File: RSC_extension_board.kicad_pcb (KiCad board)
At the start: 2 copper layers, 65 x 56.5 mm, 110 parts, among them J1 NPTC202KFMS-RC, J10 Conn_01x04, J11 Conn_01x03, J12 Conn_01x03, J13 Conn_01x10, J16 USB_C_Receptacle_PowerOnly_6P, J2 Conn_01x02, J4 TSM-120-01-L-DH-A-K-TR, J5 Conn_01x02, J6 Conn_01x03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

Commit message: generic 2.54mm headers and testPads excluded from BOM
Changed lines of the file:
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@@
 		(sheetname "/Buck converter/")
 		(sheetfile "buck_converter.kicad_sch")
-		(attr smd)
+		(attr smd dnp)
 		(fp_line
 			(start -0.254724 0.5225)
@@
 		(sheetname "/")
 		(sheetfile "RSC_extension_board.kicad_sch")
-		(attr through_hole)
+		(attr through_hole exclude_from_bom)
 		(fp_line
 			(start -1.33 24.19)
@@
 		(sheetname "/Buck converter/")
 		(sheetfile "buck_converter.kicad_sch")
-		(attr smd)
+		(attr smd dnp)
 		(fp_line
 			(start -0.254724 -0.5225)
@@
 		(sheetname "/Buck converter/")
 		(sheetfile "buck_converter.kicad_sch")
-		(attr smd)
+		(attr smd dnp)
 		(fp_line
 			(start -0.254724 0.5225)
@@
 		(sheetname "/")
 		(sheetfile "RSC_extension_board.kicad_sch")
-		(attr through_hole)
+		(attr through_hole exclude_from_bom)
 		(fp_line
 			(start -1.38 6.46)
@@
 		(sheetname "/")
 		(sheetfile "RSC_extension_board.kicad_sch")
-		(attr through_hole)
+		(attr through_hole exclude_from_bom)
 		(fp_line
 			(start -1.38 6.46)
@@
 		(property "Reference" "L1"
 			(at 0 0 90)
-			(layer "Cmts.User")
+			(layer "F.SilkS")
 			(effects
 				(font
@@
 		(sheetname "/Buck converter/")
 		(sheetfile "buck_converter.kicad_sch")
-		(attr smd)
+		(attr smd dnp)
 		(fp_line
 			(start -0.254724 -0.5225)
@@
 		(sheetname "/")
 		(sheetfile "RSC_extension_board.kicad_sch")
-		(attr through_hole)
+		(attr through_hole exclude_from_bom)
 		(fp_line
 			(start -1.38 -1.38)
@@
 		(sheetname "/")
 		(sheetfile "RSC_extension_board.kicad_sch")
-		(attr through_hole)
+		(attr through_hole exclude_from_bom)
 		(fp_line
 			(start -1.38 6.46)
@@
 		(sheetname "/Buck converter/")
 		(sheetfile "buck_converter.kicad_sch")
-		(attr smd)
+		(attr smd dnp)
 		(fp_line
 			(start -0.254724 -0.5225)
@@
 		(property "Reference" "L2"
 			(at 0 0 90)
-			(layer "Cmts.User")
+			(layer "F.SilkS")
 			(effects
 				(font
@@
 		(sheetname "/")
 		(sheetfile "RSC_extension_board.kicad_sch")
-		(attr through_hole)
+		(attr through_hole exclude_from_bom)
 		(fp_line
 			(start -1.38 6.46)
@@
 		(sheetname "/USB_power/")
 		(sheetfile "USB_power.kicad_sch")
-		(attr through_hole)
+		(attr through_hole exclude_from_bom)
 		(fp_line
 			(start -1.38 -1.38)
@@
 		(sheetname "/")
 		(sheetfile "RSC_extension_board.kicad_sch")
-		(attr through_hole)
+		(attr through_hole exclude_from_bom)
 		(fp_line
 			(start -1.38 -1.38)
@@
 		(sheetname "/Buck converter/")
 		(sheetfile "buck_converter.kicad_sch")
-		(attr smd)
+		(attr smd dnp)
 		(fp_line
 			(start -0.254724 0.5225)
@@
 		(sheetname "/")
 		(sheetfile "RSC_extension_board.kicad_sch")
-		(attr through_hole)
+		(attr through_hole exclude_from_bom)
 		(fp_line
 			(start -1.38 6.46)
@@
 		(sheetname "/")
 		(sheetfile "RSC_extension_board.kicad_sch")
-		(attr board_only exclude_from_pos_files)
+		(attr board_only exclude_from_pos_files exclude_from_bom)
 		(fp_poly
 			(pts
@@
 		(property "Reference" "J4"
 			(at -1.27 -4.19 0)
-			(layer "Cmts.User")
+			(layer "F.SilkS")
 			(effects
 				(font
@@
 		(sheetname "/")
 		(sheetfile "RSC_extension_board.kicad_sch")
-		(attr through_hole)
+		(attr through_hole exclude_from_bom)
 		(fp_line
 			(start -1.38 -1.38)
@@
 		(sheetname "/Buck converter/")
 		(sheetfile "buck_converter.kicad_sch")
-		(attr exclude_from_pos_files)
+		(attr exclude_from_pos_files exclude_from_bom)
 		(fp_circle
 			(center 0 0)
@@
 		(sheetname "/Buck converter/")
 		(sheetfile "buck_converter.kicad_sch")
-		(attr exclude_from_pos_files)
+		(attr exclude_from_pos_files exclude_from_bom)
 		(fp_circle
 			(center 0 0)
@@
 		(sheetname "/Buck converter/")
 		(sheetfile "buck_converter.kicad_sch")
-		(attr exclude_from_pos_files)
+		(attr exclude_from_pos_files exclude_from_bom)
 		(fp_circle
 			(center 0 0)
@@
 		(sheetname "/Buck converter/")
 		(sheetfile "buck_converter.kicad_sch")
-		(attr exclude_from_pos_files)
+		(attr exclude_from_pos_files exclude_from_bom)
 		(fp_circle
 			(center 0 0)
@@
 		(sheetname "/Buck converter/")
 		(sheetfile "buck_converter.kicad_sch")
-		(attr exclude_from_pos_files)
+		(attr exclude_from_pos_files exclude_from_bom)
 		(fp_circle
 			(center 0 0)
@@
 		(sheetname "/Buck converter/")
 		(sheetfile "buck_converter.kicad_sch")
-		(attr exclude_from_pos_files)
+		(attr exclude_from_pos_files exclude_from_bom)
 		(fp_circle
 			(center 0 0)
@@
 		(sheetname "/Buck converter/")
 		(sheetfile "buck_converter.kicad_sch")
-		(attr exclude_from_pos_files)
+		(attr exclude_from_pos_files exclude_from_bom)
 		(fp_circle
 			(center 0 0)
@@
 		(sheetname "/Buck converter/")
 		(sheetfile "buck_converter.kicad_sch")
-		(attr exclude_from_pos_files)
+		(attr exclude_from_pos_files exclude_from_bom)
 		(fp_circle
 			(center 0 0)
@@
 		(sheetname "/Buck converter/")
 		(sheetfile "buck_converter.kicad_sch")
-		(attr exclude_from_pos_files)
+		(attr exclude_from_pos_files exclude_from_bom)
 		(fp_circle
 			(center 0 0)
@@
 		(sheetname "/Buck converter/")
 		(sheetfile "buck_converter.kicad_sch")
-		(attr exclude_from_pos_files)
+		(attr exclude_from_pos_files exclude_from_bom)
 		(fp_circle
 			(center 0 0)
@@
 		(sheetname "/Buck converter/")
 		(sheetfile "buck_converter.kicad_sch")
-		(attr exclude_from_pos_files)
+		(attr exclude_from_pos_files exclude_from_bom)
 		(fp_circle
 			(center 0 0)
@@
 		(sheetname "/Buck converter/")
 		(sheetfile "buck_converter.kicad_sch")
-		(attr exclude_from_pos_files)
+		(attr exclude_from_pos_files exclude_from_bom)
 		(fp_circle
 			(center 0 0)
@@
 		(sheetname "/Buck converter/")
 		(sheetfile "buck_converter.kicad_sch")
-		(attr exclude_from_pos_files)
+		(attr exclude_from_pos_files exclude_from_bom)
 		(fp_circle
 			(center 0 0)
@@
 		(sheetname "/Buck converter/")
 		(sheetfile "buck_converter.kicad_sch")
-		(attr exclude_from_pos_files)
+		(attr exclude_from_pos_files exclude_from_bom)
 		(fp_circle
 			(center 0 0)
@@
 		(sheetname "/Buck converter/")
 		(sheetfile "buck_converter.kicad_sch")
-		(attr exclude_from_pos_files)
+		(attr exclude_from_pos_files exclude_from_bom)
 		(fp_circle
 			(center 0 0)
@@
 		(sheetname "/Buck converter/")
 		(sheetfile "buck_converter.kicad_sch")
-		(attr exclude_from_pos_files)
+		(attr exclude_from_pos_files exclude_from_bom)
 		(fp_circle
 			(center 0 0)

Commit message: J4 connector had correct footprint but false component name
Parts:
- J4: value TSM-120-01-L-DH-A-K-TR -> TSM-120-02-F-DH
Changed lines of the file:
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@@
 			)
 		)
-		(property "Value" "TSM-120-01-L-DH-A-K-TR"
+		(property "Value" "TSM-120-02-F-DH"
 			(at 0 0 0)
 			(layer "F.SilkS")
@@
 			)
 		)
-		(property "Manufacturer_Part_Number" "TSM-120-01-L-DH-A-K-TR"
+		(property "Manufacturer_Part_Number" "TSM-120-02-F-DH "
 			(at 0 0 0)
 			(unlocked yes)
@@
 			)
 		)
-		(property "Mouser Part Number" "200-TSM12001LDHAKTR"
+		(property "Mouser Part Number" "200-TSM12002FDH "
 			(at 0 0 0)
 			(unlocked yes)
@@
 			)
 		)
-		(property "Mouser Price/Stock" "https://www.mouser.co.uk/ProductDetail/Samtec/TSM-120-01-L-DH-A-K-TR?qs=Cqqh%252BS766wkIdpcdtjp1jQ%3D%3D"
+		(property "Mouser Price/Stock" ""
 			(at 0 0 0)
 			(unlocked yes)

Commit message: correct feedback resistors on buck converters
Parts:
- RFBB1, RFBB2: value DNP -> 20k
- RFBT1, RFBT2: value SHUNT -> 82k
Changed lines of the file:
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@@
 			)
 		)
-		(property "Value" "DNP"
+		(property "Value" "20k"
 			(at 0 1.43 90)
 			(layer "F.Fab")
@@
 		(sheetname "/Buck converter/")
 		(sheetfile "buck_converter.kicad_sch")
-		(attr smd dnp)
+		(attr smd)
 		(fp_line
 			(start -0.254724 -0.5225)
@@
 			)
 		)
-		(property "Value" "DNP"
+		(property "Value" "20k"
 			(at 0 1.43 0)
 			(layer "F.Fab")
@@
 		(sheetname "/Buck converter/")
 		(sheetfile "buck_converter.kicad_sch")
-		(attr smd dnp)
+		(attr smd)
 		(fp_line
 			(start -0.254724 0.5225)
@@
 			(at 0 0 90)
 			(layer "F.SilkS")
+			(hide yes)
 			(effects
 				(font
@@
 			)
 		)
-		(property "Value" "SHUNT"
+		(property "Value" "82k"
 			(at 0 1.43 90)
 			(layer "F.Fab")
@@
 			(at 0 0 90)
 			(layer "F.SilkS")
+			(hide yes)
 			(effects
 				(font
@@
 			)
 		)
-		(property "Manufacturer_Part_Number" "TSM-120-02-F-DH "
+		(property "Manufacturer_Part_Number" "TSM-120-02-F-DH"
 			(at 0 0 0)
 			(unlocked yes)
@@
 			)
 		)
-		(property "Mouser Part Number" "200-TSM12002FDH "
+		(property "Mouser Part Number" "200-TSM12002FDH"
 			(at 0 0 0)
 			(unlocked yes)
@@
 			)
 		)
-		(property "Value" "SHUNT"
+		(property "Value" "82k"
 			(at 0 1.43 90)
 			(layer "F.Fab")

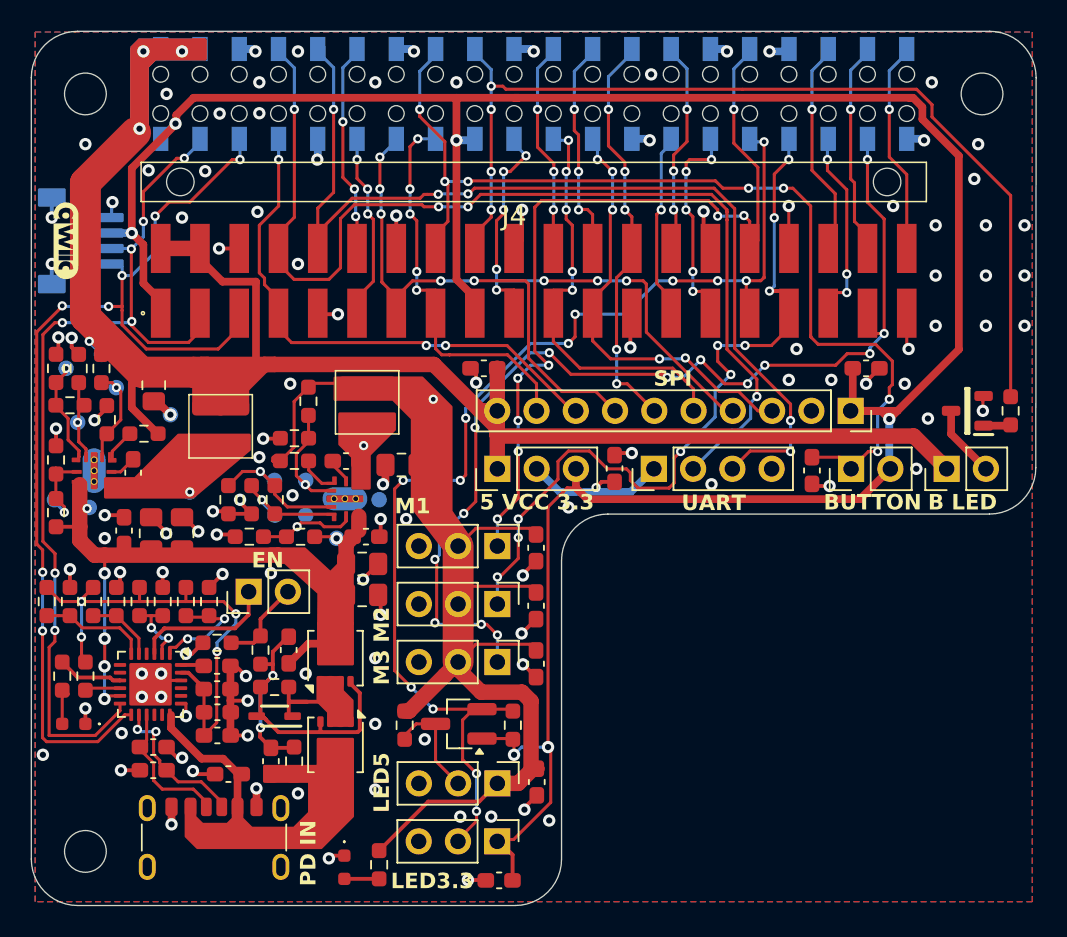
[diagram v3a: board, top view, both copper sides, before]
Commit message: Started Rev B: white power LED, USB slightly over edge
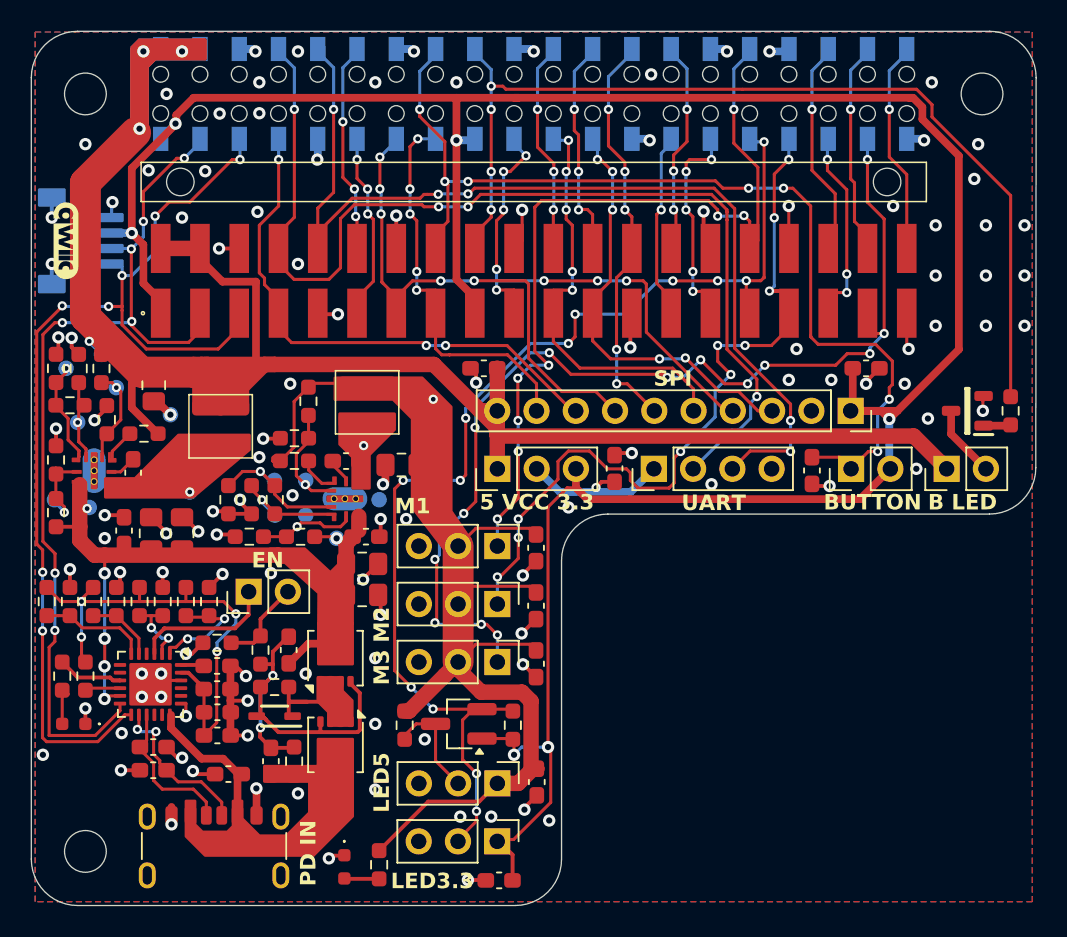
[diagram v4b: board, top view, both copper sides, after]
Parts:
- LED1: value KR_EELP41.22-Q1S1-36-A8J8-020-R18 -> KW_EELP41.RU-S1U1-3K6L-3X4X-5-R18; footprint KR_EELP41.22-Q1S1-36-A8J8-020-R18:KREELP4122Q1S136A8J8020R18 -> KW_EELP41.RU-S1U1-3K6L-3X4X-5-R18:KWEELP41RUS1U13K6L3X4X5R18
- R1: value 150 -> 1k
- moved J16 0.55 mm to (106.8, 98.2)
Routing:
- net Net-(J16-CC2): track 9.95 -> 10.5 mm
- net Net-(J16-CC1): track 8.95 -> 9.50 mm
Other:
- board text added: "RSC Adapter, Rev B, Raiko Torga, 2026"
- board text removed: "RSC Adapter, Rev A, Raiko Torga, 2026"

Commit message: new logo. lmr has 1st pin marking. pinout on silkscreen.
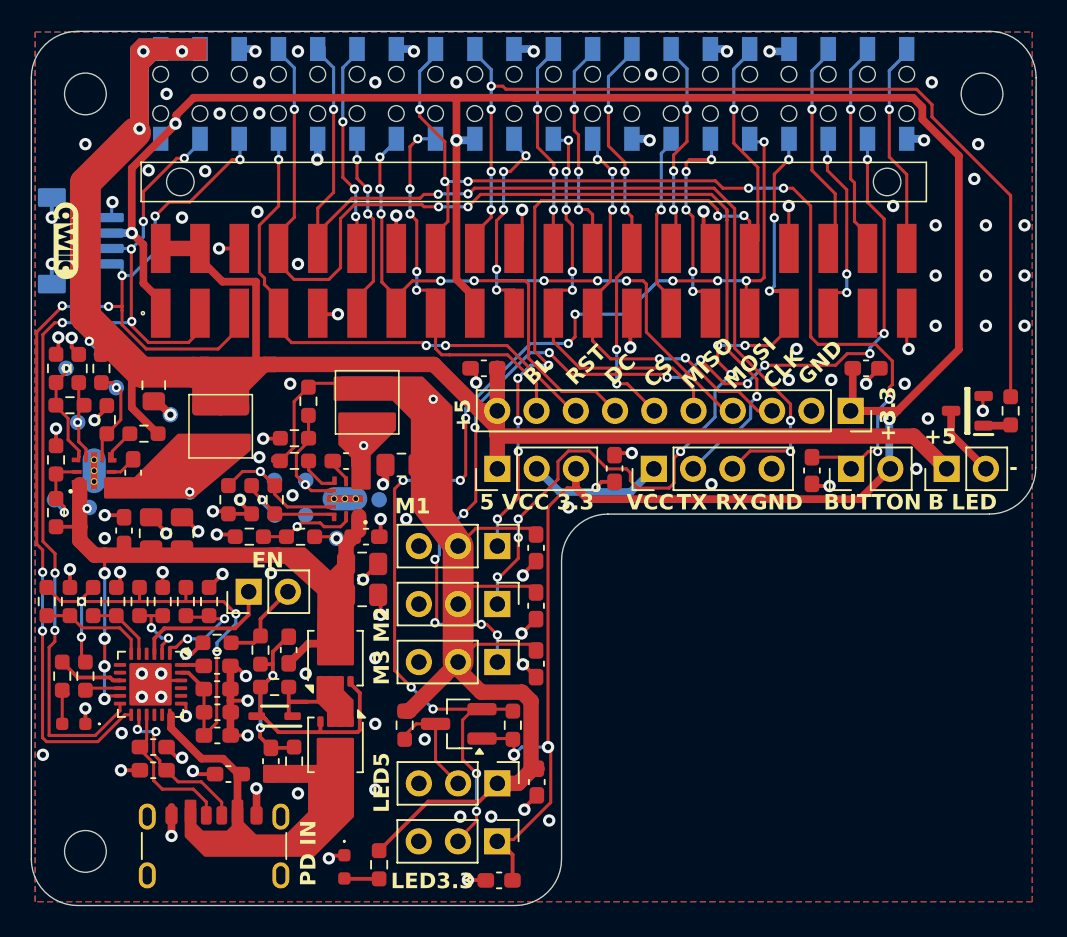
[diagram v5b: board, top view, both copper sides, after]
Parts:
- moved G*** 0.90 mm to (114.8, 60.2)
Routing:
- net GND: track 93.8 -> 94.5 mm
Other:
- board text added: "+"
- board text added: "+3.3"
- board text added: "+5"
- board text added: "-"
- board text added: "BL"
- board text added: "CLK"
- board text added: "CS"
- board text added: "DC"
- board text added: "GND"
- board text added: "MISO"
- board text added: "MOSI"
- board text added: "PWM"
- board text added: "RST"
- board text added: "RX"
- board text added: "S"
- board text added: "SCL"
- board text added: "SDA"
- board text added: "TX"
- board text added: "VCC"
- board text removed: "SPI"
- board text removed: "UART"

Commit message: silkscreen: torxhat, OSHW Certification Mark
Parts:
- added G***: LOGO, LOGO, B.Cu at (141.2, 65.5)
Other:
- board text added: "torxHAT, Rev B, Raiko Torga, 2026"
- board text removed: "RSC Adapter, Rev B, Raiko Torga, 2026"

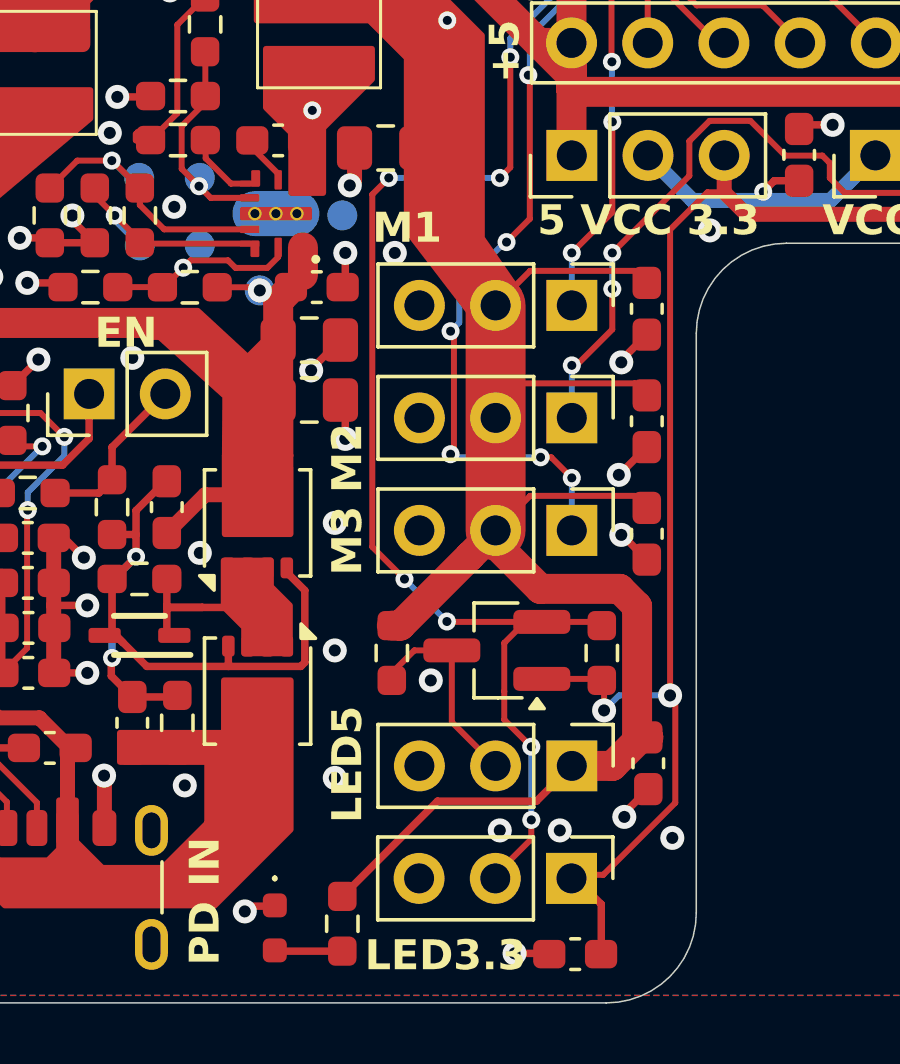
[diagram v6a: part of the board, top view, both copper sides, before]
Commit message: 1k led resistors. top silkscreen
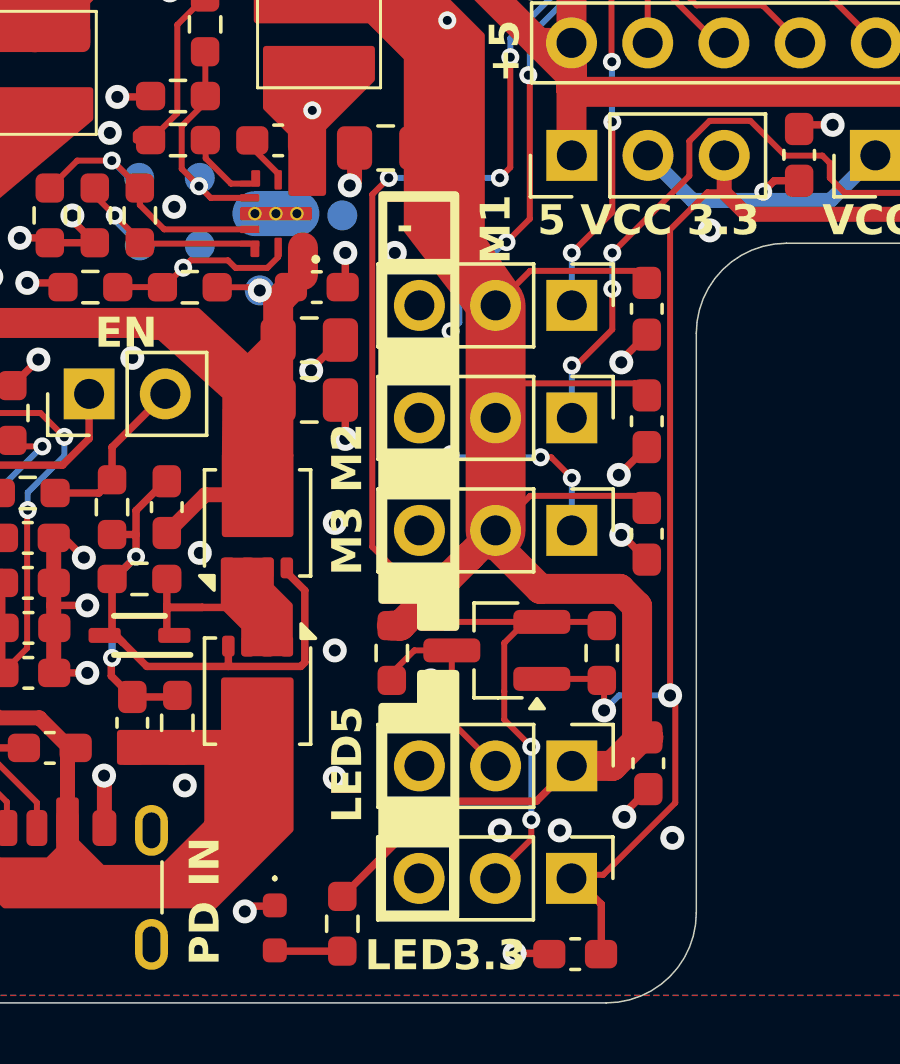
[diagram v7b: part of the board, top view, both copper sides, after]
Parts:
- R17: value 68 -> 1k
